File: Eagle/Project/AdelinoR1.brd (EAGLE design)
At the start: 47 x 53.3 mm, 63 parts, among them J1 DC-044-A, J2 YELLOW-8P-2.54, J3 YELLOW-6P-2.54, J4 YELLOW-8P-2.54, J5 YELLOW-8P-2.54, J6 4P-2.0, J7 YELLOW-2X3P-2.54, J8 4P-2.0, Q1 NCE3407A, Q2 CJ2305, SW1 TS-1101F, U1 CJT1117-5.0-SOT223, U2 CJT1117-3.3-SOT223, U3 ESP-12F / OPL: 317060163 / SM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, U4 ATMEGA32U4-TQFP44, X1 306010049_XTAL_16MHZ-3225_4P

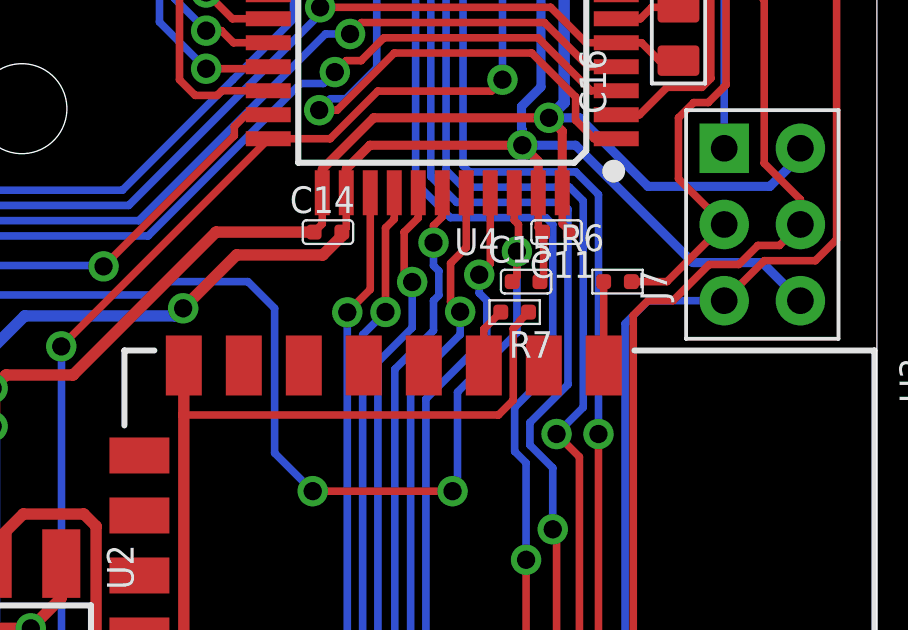
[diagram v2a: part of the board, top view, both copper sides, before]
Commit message: Now SCK drives CHIP_EN instead of RST; RST pulled high using 4K7.
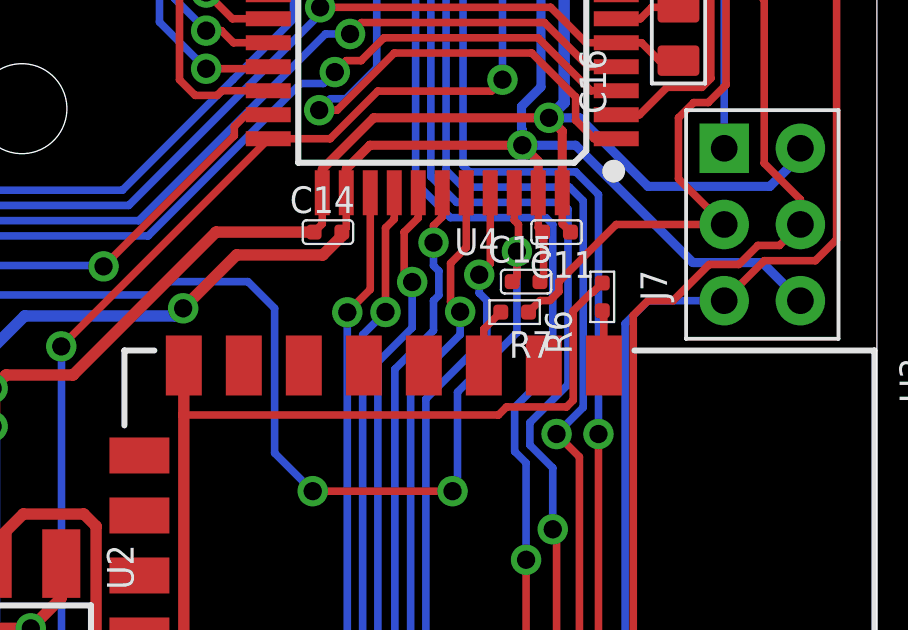
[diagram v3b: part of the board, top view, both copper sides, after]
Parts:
- moved R6 0.72 mm to (37.8, 25.5), turned to 0 degrees
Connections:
- net +3V3: now also R6.1; no longer R7.1
- net SCK: now also R7.1; no longer R6.1
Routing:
- net SCK: track 17.7 -> 21.7 mm
- net +3V3: track 103.4 -> 106.6 mm
- net N$14: track 2.80 -> 1.85 mm
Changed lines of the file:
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@@
 <attribute name="VALUE" x="0.808" y="28.283" size="0.635" layer="27" ratio="10"/>
 </element>
-<element name="R6" library="Seeed-Resistor" package="R0402" value="4.7K" x="38.354" y="26.035" smashed="yes" rot="R270">
-<attribute name="MPN" value="RC0402JR-074K7L" x="38.354" y="26.035" size="1.778" layer="27" rot="R270" display="off"/>
-<attribute name="NAME" x="36.449" y="27.051" size="0.889" layer="25" ratio="11"/>
-<attribute name="VALUE" value="4.7K" x="36.749" y="24.6" size="0.635" layer="27" ratio="10"/>
+<element name="R6" library="Seeed-Resistor" package="R0402" value="4.7K" x="37.846" y="25.527" smashed="yes">
+<attribute name="MPN" value="RC0402JR-074K7L" x="37.846" y="25.527" size="1.778" layer="27" display="off"/>
+<attribute name="NAME" x="36.83" y="23.622" size="0.889" layer="25" ratio="11" rot="R90"/>
+<attribute name="VALUE" value="4.7K" x="39.281" y="23.922" size="0.635" layer="27" ratio="10" rot="R90"/>
 </element>
 <element name="R9" library="Seeed-Resistor" package="R0402" value="4.7K" x="35.56" y="5.588" smashed="yes" rot="R270">
@@
 <wire x1="10.16" y1="8.6995" x2="11.3665" y2="9.906" width="0.508" layer="1"/>
 <wire x1="11.3665" y1="9.906" x2="12.827" y2="9.906" width="0.508" layer="1"/>
-<wire x1="35.8595" y1="27.686" x2="35.712" y2="27.8335" width="0.254" layer="1"/>
-<wire x1="35.712" y1="28.998" x2="35.712" y2="27.8335" width="0.254" layer="1"/>
+<wire x1="35.712" y1="27.8335" x2="35.8595" y2="27.686" width="0.254" layer="1"/>
 <wire x1="29.312" y1="27.8335" x2="29.1645" y2="27.686" width="0.254" layer="1"/>
 <wire x1="29.312" y1="28.998" x2="29.312" y2="27.8335" width="0.254" layer="1"/>
@@
 <wire x1="4.399" y1="39.468" x2="6.575" y2="39.468" width="0.381" layer="1"/>
 <wire x1="6.575" y1="39.468" x2="6.604" y2="39.497" width="0.381" layer="1"/>
+<wire x1="35.712" y1="28.998" x2="35.712" y2="27.8335" width="0.254" layer="1"/>
 </signal>
 <signal name="N$1">
@@
 <wire x1="1.778" y1="5.588" x2="1.148" y2="6.218" width="0.254" layer="1"/>
 <wire x1="1.148" y1="21.336" x2="1.148" y2="6.218" width="0.254" layer="1"/>
-<contactref element="R7" pad="1"/>
-<wire x1="35.0935" y1="24.68440625" x2="35.0935" y2="24.725" width="0.254" layer="1"/>
-<wire x1="35.0935" y1="24.725" x2="35.3875" y2="25.019" width="0.254" layer="1"/>
-<wire x1="34.878" y1="24.46890625" x2="35.0935" y2="24.68440625" width="0.254" layer="1"/>
-<wire x1="34.878" y1="22.0821875" x2="34.878" y2="24.46890625" width="0.254" layer="1"/>
-<wire x1="34.3858125" y1="21.59" x2="34.878" y2="22.0821875" width="0.254" layer="1"/>
-<wire x1="23.897" y1="21.59" x2="34.3858125" y2="21.59" width="0.254" layer="1"/>
+<wire x1="34.3858125" y1="21.59" x2="23.897" y2="21.59" width="0.254" layer="1"/>
 <wire x1="1.9505" y1="22.098" x2="1.91" y2="22.098" width="0.254" layer="1"/>
 <wire x1="1.91" y1="22.098" x2="1.148" y2="21.336" width="0.254" layer="1"/>
@@
 <wire x1="20.9725" y1="17.88311875" x2="20.9725" y2="13.0985" width="0.381" layer="1"/>
 <wire x1="20.9725" y1="13.0985" x2="18.161" y2="10.287" width="0.381" layer="1"/>
+<contactref element="R6" pad="1"/>
+<wire x1="37.846" y1="25.9895" x2="37.552" y2="25.6955" width="0.254" layer="1"/>
+<wire x1="37.552" y1="25.6955" x2="37.51140625" y2="25.6955" width="0.254" layer="1"/>
+<wire x1="36.878" y1="22.0821875" x2="36.6548125" y2="21.859" width="0.254" layer="1"/>
+<wire x1="37.51140625" y1="25.6955" x2="36.878" y2="25.06209375" width="0.254" layer="1"/>
+<wire x1="36.878" y1="25.06209375" x2="36.878" y2="22.0821875" width="0.254" layer="1"/>
+<wire x1="34.6548125" y1="21.859" x2="34.3858125" y2="21.59" width="0.254" layer="1"/>
+<wire x1="36.6548125" y1="21.859" x2="34.6548125" y2="21.859" width="0.254" layer="1"/>
 </signal>
 <signal name="N$9">
@@
 <contactref element="U4" pad="9"/>
 <contactref element="J7" pad="2"/>
-<contactref element="R6" pad="1"/>
 <wire x1="38.312" y1="37.198" x2="38.481" y2="37.029" width="0.254" layer="1"/>
 <wire x1="41.9735" y1="35.98084375" x2="41.9735" y2="32.59915625" width="0.254" layer="1"/>
@@
 <wire x1="40.386" y1="31.496" x2="40.386" y2="29.464" width="0.254" layer="1"/>
 <wire x1="40.386" y1="29.464" x2="41.91" y2="27.94" width="0.254" layer="1"/>
-<wire x1="41.91" y1="27.94" x2="40.005" y2="26.035" width="0.254" layer="1"/>
-<wire x1="40.005" y1="26.035" x2="38.8165" y2="26.035" width="0.254" layer="1"/>
+<contactref element="R7" pad="1"/>
+<wire x1="41.91" y1="27.94" x2="38.3085" y2="27.94" width="0.254" layer="1"/>
+<wire x1="38.3085" y1="27.94" x2="36.3995" y2="26.031" width="0.254" layer="1"/>
+<wire x1="36.3995" y1="26.031" x2="36.3995" y2="25.70040625" width="0.254" layer="1"/>
+<wire x1="36.3995" y1="25.70040625" x2="36.10309375" y2="25.404" width="0.254" layer="1"/>
+<wire x1="36.10309375" y1="25.404" x2="35.7725" y2="25.404" width="0.254" layer="1"/>
+<wire x1="35.7725" y1="25.404" x2="35.3875" y2="25.019" width="0.254" layer="1"/>
 </signal>
 <signal name="MOSI">
@@
 <contactref element="R6" pad="2"/>
 <contactref element="U3" pad="1"/>
-<wire x1="37.8915" y1="26.035" x2="37.8915" y2="23.2455" width="0.254" layer="1"/>
-<wire x1="37.8915" y1="23.2455" x2="37.897" y2="23.24" width="0.254" layer="1"/>
+<wire x1="37.846" y1="25.0645" x2="37.897" y2="25.0135" width="0.254" layer="1"/>
+<wire x1="37.897" y1="25.0135" x2="37.897" y2="23.24" width="0.254" layer="1"/>
 </signal>
 <signal name="N$17">

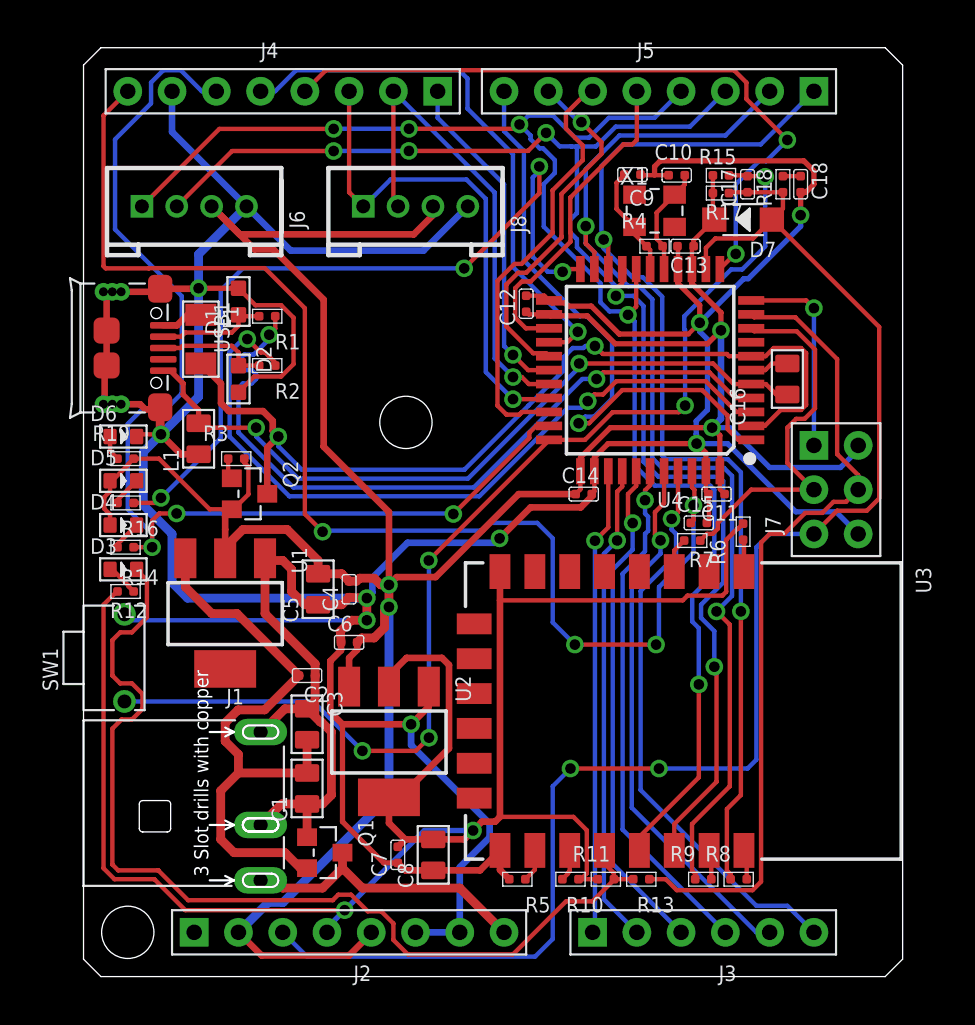
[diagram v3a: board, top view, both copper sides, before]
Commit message: Change ACT_LED to PB0; change ESP_EN to PD5; change WIFI led to GPIO2.
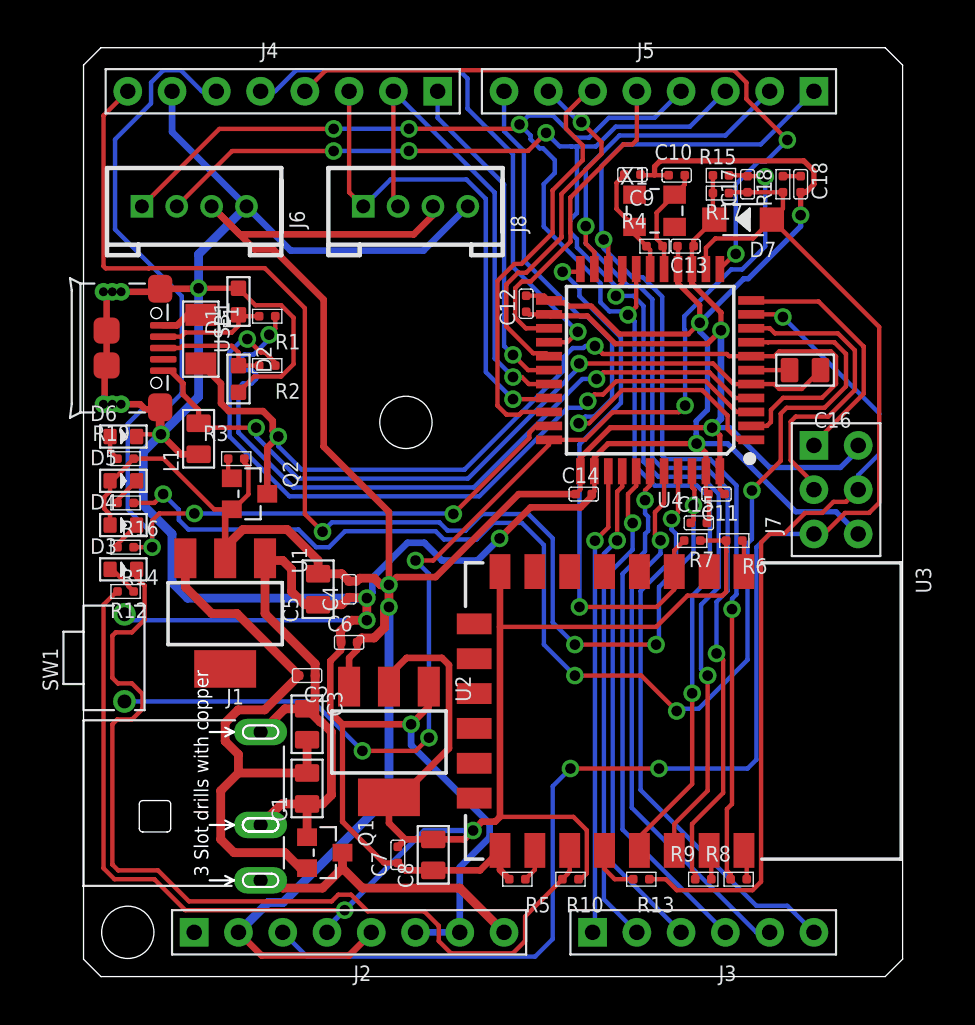
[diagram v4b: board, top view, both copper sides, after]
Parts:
- removed R11: 10K, Seeed-Resistor:R0402
- moved C16 1.14 mm to (41.4, 34.8), turned to 270 degrees
- moved R6 0.72 mm to (37.3, 25.0), turned to 90 degrees
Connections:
- removed net N$11: R10.1, U3.17
- removed net SS: U4.8
- removed net TXLED: R16.2, U4.22
- new net ACT_LED: R16.2, U4.8
- new net GPIO2: D3.-, R10.1, U3.17
- net +3V3: now also R7.1; no longer R11.2
- net ESP_EN: now also U4.22
- net GPIO0: no longer D3.-, R11.1
- net SCK: no longer R7.1
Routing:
- net ACT_LED: track 0.00 -> 73.9 mm, vias 0 -> 4
- net GPIO0: track 57.1 -> 2.95 mm
- net GPIO2: track 0.00 -> 54.0 mm
- net TXLED: track 45.6 -> 0.00 mm, vias 4 -> 0
- net ESP_EN: track 2.01 -> 31.6 mm, vias 0 -> 2
- net SCK: track 21.7 -> 17.7 mm
- net VUSB: track 52.7 -> 55.6 mm
- net MISO: track 11.7 -> 14.4 mm, vias 1 -> 0
- net UGND: track 43.1 -> 45.3 mm
- net N$11: track 1.83 -> 0.00 mm
- net PIN_D2: track 85.3 -> 84.0 mm
- net RSTAT: track 65.1 -> 66.3 mm
- net PIN_D1: track 63.4 -> 62.3 mm
- net PIN_D3: track 88.9 -> 88.0 mm
- net GND: track 278.8 -> 279.6 mm
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
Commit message: Adelino X1 final design.
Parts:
- added R11: 47K, Seeed-Resistor:R0402
- added R20, R21: 1K, Seeed-Resistor:R0402
- added U$1, U$2: MMBT3904LT1G, Seeed-Transistor:SOT-23
- R10, R6, R7: value 4.7K -> 10K 1/16W
- R13, R8, R9: value 4.7K -> 1K
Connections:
- new net N$16: R20.2, U$1.1
- new net N$21: R21.2, U$2.1
- new net STANDBY1: U$1.3
- new net STANDBY2: U$2.3
- net +3V3: now also R11.2
- net GND: now also U$1.2, U$2.2
- net GPIO0: now also R11.1
- net PIN_D13: now also R21.1
- net PIN_D5: now also R20.1
- net RESET: now also U3.4
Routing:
- net RESET: track 87.3 -> 108.2 mm, vias 2 -> 3
- net PIN_D13: track 64.1 -> 81.7 mm, vias 3 -> 4
- net GND: track 279.6 -> 292.8 mm
- net PIN_D5: track 24.7 -> 29.3 mm, vias 0 -> 1
- net +5V: track 175.9 -> 172.4 mm
- net STANDBY2: track 0.00 -> 1.78 mm, vias 0 -> 1
- net STANDBY1: track 0.00 -> 1.78 mm, vias 0 -> 1
- net N$21: track 0.00 -> 1.57 mm
- net N$16: track 0.00 -> 1.36 mm
- net GPIO0: track 2.95 -> 4.00 mm, vias 0 -> 1
- net +3V3: track 106.2 -> 106.9 mm
- net ACT_LED: track 73.9 -> 74.7 mm

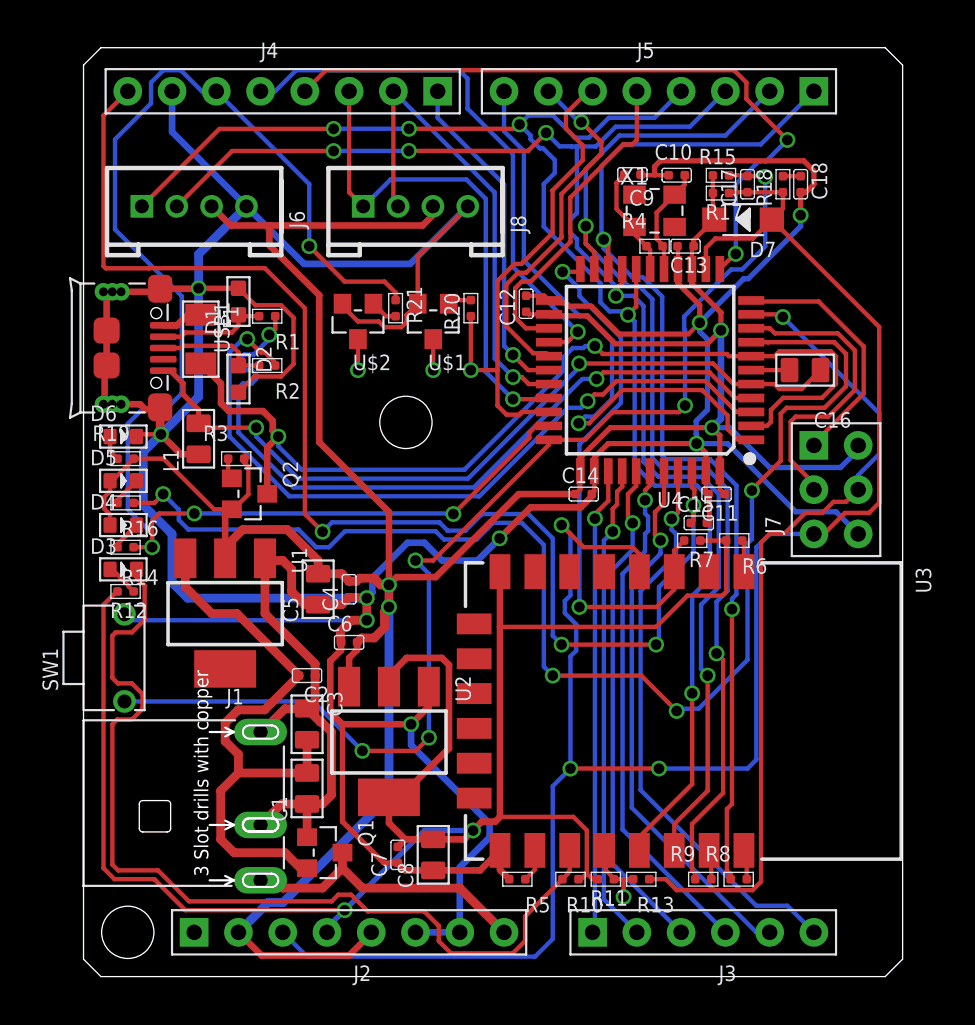
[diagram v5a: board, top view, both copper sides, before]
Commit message: Add spare vias for SPI.
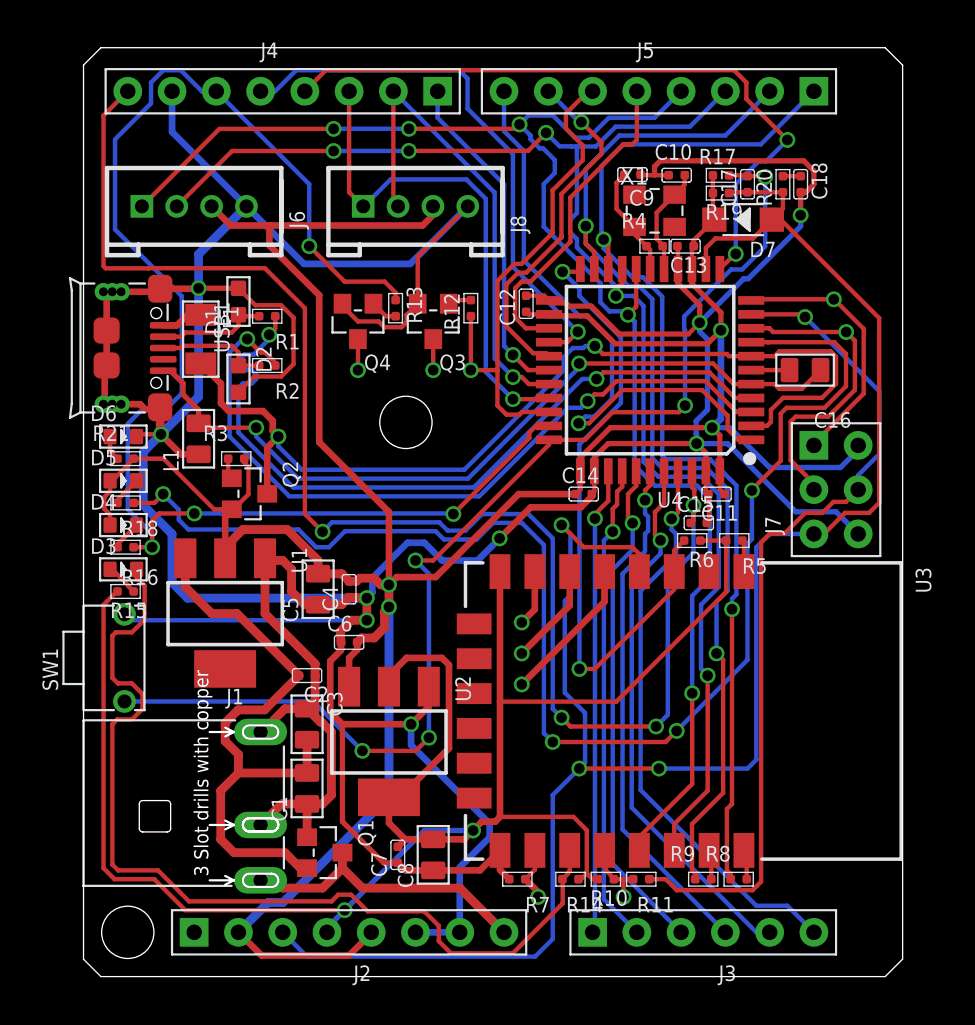
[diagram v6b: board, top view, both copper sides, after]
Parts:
- R10: value 10K 1/16W -> 47K
- R11: value 47K -> 1K
- R12: value 470R -> 1K
- R14: value 1K -> 10K 1/16W
- R15: value 100K -> 470R
- R18: value 10K -> 1K
- R19: value 1K -> 100K
- R20: value 1K -> 10K
- R5: value 10K -> 10K 1/16W
- R7: value 10K 1/16W -> 10K
- moved R18 41.9 mm to (2.41, 27.2), turned to 90 degrees
- moved R15 41.7 mm to (2.41, 22.1), turned to 270 degrees
- moved R19 37.4 mm to (36.6, 45.0)
- moved R13 35.7 mm to (17.9, 38.4), turned to 0 degrees
- moved R14 31.9 mm to (27.9, 5.59)
- moved R12 25.6 mm to (22.2, 38.4), turned to 180 degrees
- moved R5 23.1 mm to (37.3, 25.0)
- moved R7 21.9 mm to (24.9, 5.59), turned to 90 degrees
- moved R20 19.3 mm to (40.1, 45.5)
- moved R21 17.7 mm to (2.41, 29.7), turned to 270 degrees
- moved R16 2.54 mm to (2.41, 24.6)
- moved R6 2.41 mm to (34.9, 25.0), turned to 270 degrees
- moved R10 2.03 mm to (30.0, 5.59), turned to 270 degrees
- moved R11 2.03 mm to (32.0, 5.59), turned to 90 degrees
- moved R17 1.02 mm to (36.6, 46.0), turned to 90 degrees
- renumbered U$1 to Q3, U$2 to Q4
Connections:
- new net HSPI_CLK: U3.5
- new net HSPI_MISO: U3.6
- new net HSPI_MOSI: U3.7
- net +3V3: now also R14.2, R15.2, R5.1; no longer R11.2, R12.2, R7.1
- net +5V: now also R17.1, R19.2, R21.1; no longer R15.1, R17.2, R19.1
- net ACT_LED: now also R18.2; no longer R16.2
- net ESP_EN: now also R6.2; no longer R7.2
- net GND: now also R7.1; no longer R5.1
- net GPIO0: now also R10.1; no longer R13.1
- net GPIO2: now also R14.1; no longer R10.1
- net MOSI: now also R11.2; no longer R13.2
- net N$12: now also R15.1; no longer R12.1
- net N$13: now also R20.2; no longer R18.2
- net N$14: now also R5.2; no longer R6.2
- net N$16: now also R12.2; no longer R20.2
- net N$21: now also R13.2; no longer R21.2
- net N$4: now also R7.2; no longer R5.2
- net N$5: now also R21.2; no longer R19.2
- net N$6: now also R18.1; no longer R16.1
- net N$8: now also R16.1; no longer R14.1
- net PIN_D13: now also R13.1, R16.2; no longer R14.2, R21.1
- net PIN_D5: now also R12.1; no longer R20.1
- net RESET: now also R19.1, R20.1; no longer R17.1, R18.1
- net RSTAT: now also R17.2; no longer R15.2
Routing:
- net PIN_AREF: track 74.7 -> 83.8 mm
- net HSPI_CLK: track 0.00 -> 8.44 mm, vias 0 -> 1
- net HSPI_MISO: track 0.00 -> 5.84 mm, vias 0 -> 1
- net ESP_EN: track 31.6 -> 36.6 mm
- net ACT_LED: track 74.7 -> 78.4 mm
- net HSPI_MOSI: track 0.00 -> 3.23 mm, vias 0 -> 1
- net +3V3: track 106.9 -> 108.7 mm
- net N$4: track 1.88 -> 3.20 mm, vias 0 -> 1
- net MOSI: track 47.7 -> 48.5 mm
- net MISO: track 14.4 -> 15.1 mm, vias 0 -> 1
- net SCK: track 17.7 -> 18.0 mm, vias 0 -> 1
